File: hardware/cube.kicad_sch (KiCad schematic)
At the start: 16 parts, among them J1 PDB, M1 GM4108H, M2 Servo, SW1 Button, U1 ESP32-DevKitC, U2 BNO085, U3 Servo buck

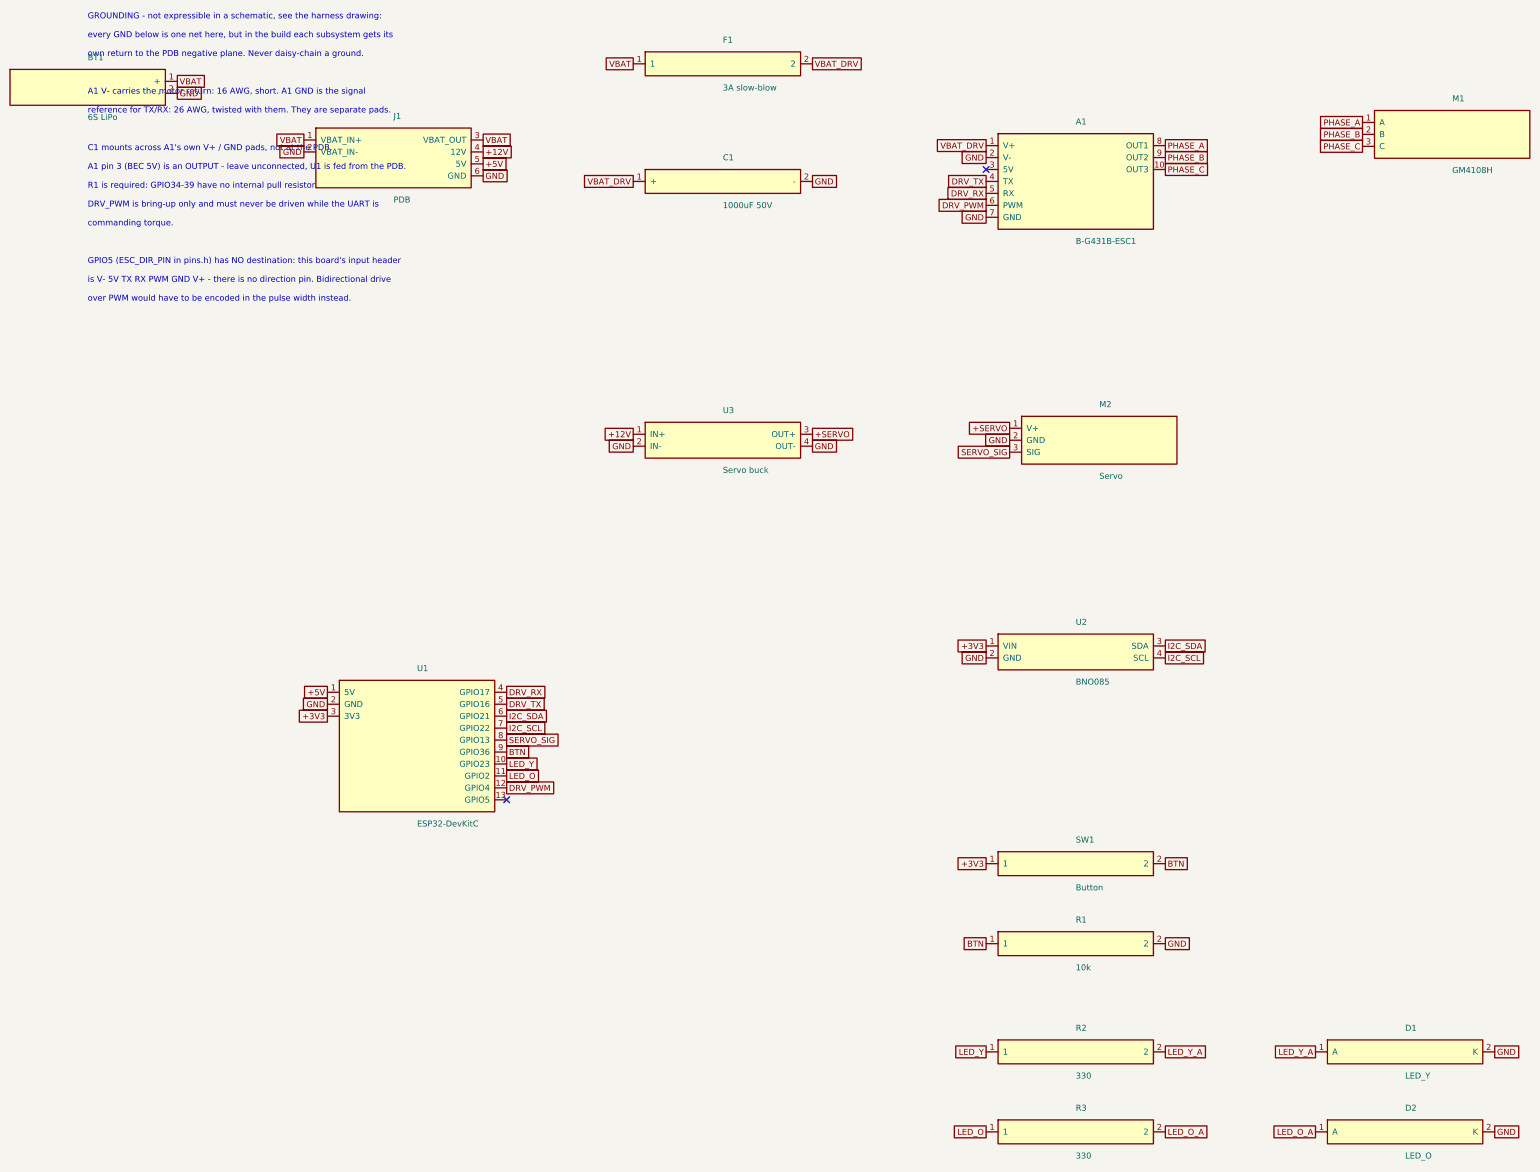
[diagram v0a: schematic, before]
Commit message: Redraw the schematic: real glyphs, drawn power chain, debug parts removed
The first sheet was a correct netlist and a poor drawing. Every part was a
rectangle and every connection was a matching pair of text labels, so the
topology could not be read - you could not see that C1 sits across the driver's
terminals, only infer it from two labels that happened to agree.

Changes:

- Passives carry their real symbols. BT1 is alternating cell plates, C1 is a
  polarised capacitor with its plates and + marker, F1 is the fuse glyph, M1 is
  a circle. The modules stay rectangles, which is correct: the PDB, driver,
  buck, IMU and ESP32 are finished boards you wire to, so a connector is the
  honest representation.

- The power chain is drawn with wires and junction dots, battery through PDB,
  fuse and bulk cap to the driver, so C1 is visibly in parallel across V+ and
  GND rather than implied.

- Rails use power symbols - a GND triangle, +5V / +3V3 / +12V bars - instead of
  text labels. Signals still travel by global label, which is ordinary practice
  and keeps the sheet legible.

- Removed the button, its pulldown, both LEDs and their series resistors. They
  are bring-up aids, not part of the machine. Removed the notes block; what it
  said about grounding belongs in the harness drawing, which is where the star
  topology and the wire gauges already live.

Both no-connects are kept, since each records a real finding: A1 pin 7 is the
BEC output and must not meet the PDB's 5 V rail, and U1 GPIO5 is ESC_DIR_PIN in
pins.h with no destination, because this driver's header has a PWM input and no
direction pin.

Checked: parentheses balanced outside strings, 159 unique UUIDs, every lib_id
defined, no duplicate symbol bodies, and all 46 part pins plus all 14 power
symbol pins terminate on a wire, a label or a no-connect - nothing dangles.
Not opened in KiCad; there is no install here.

Co-Authored-By: Claude Opus 5 <noreply@anthropic.com>
Claude-Session: https://claude.ai/code/s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
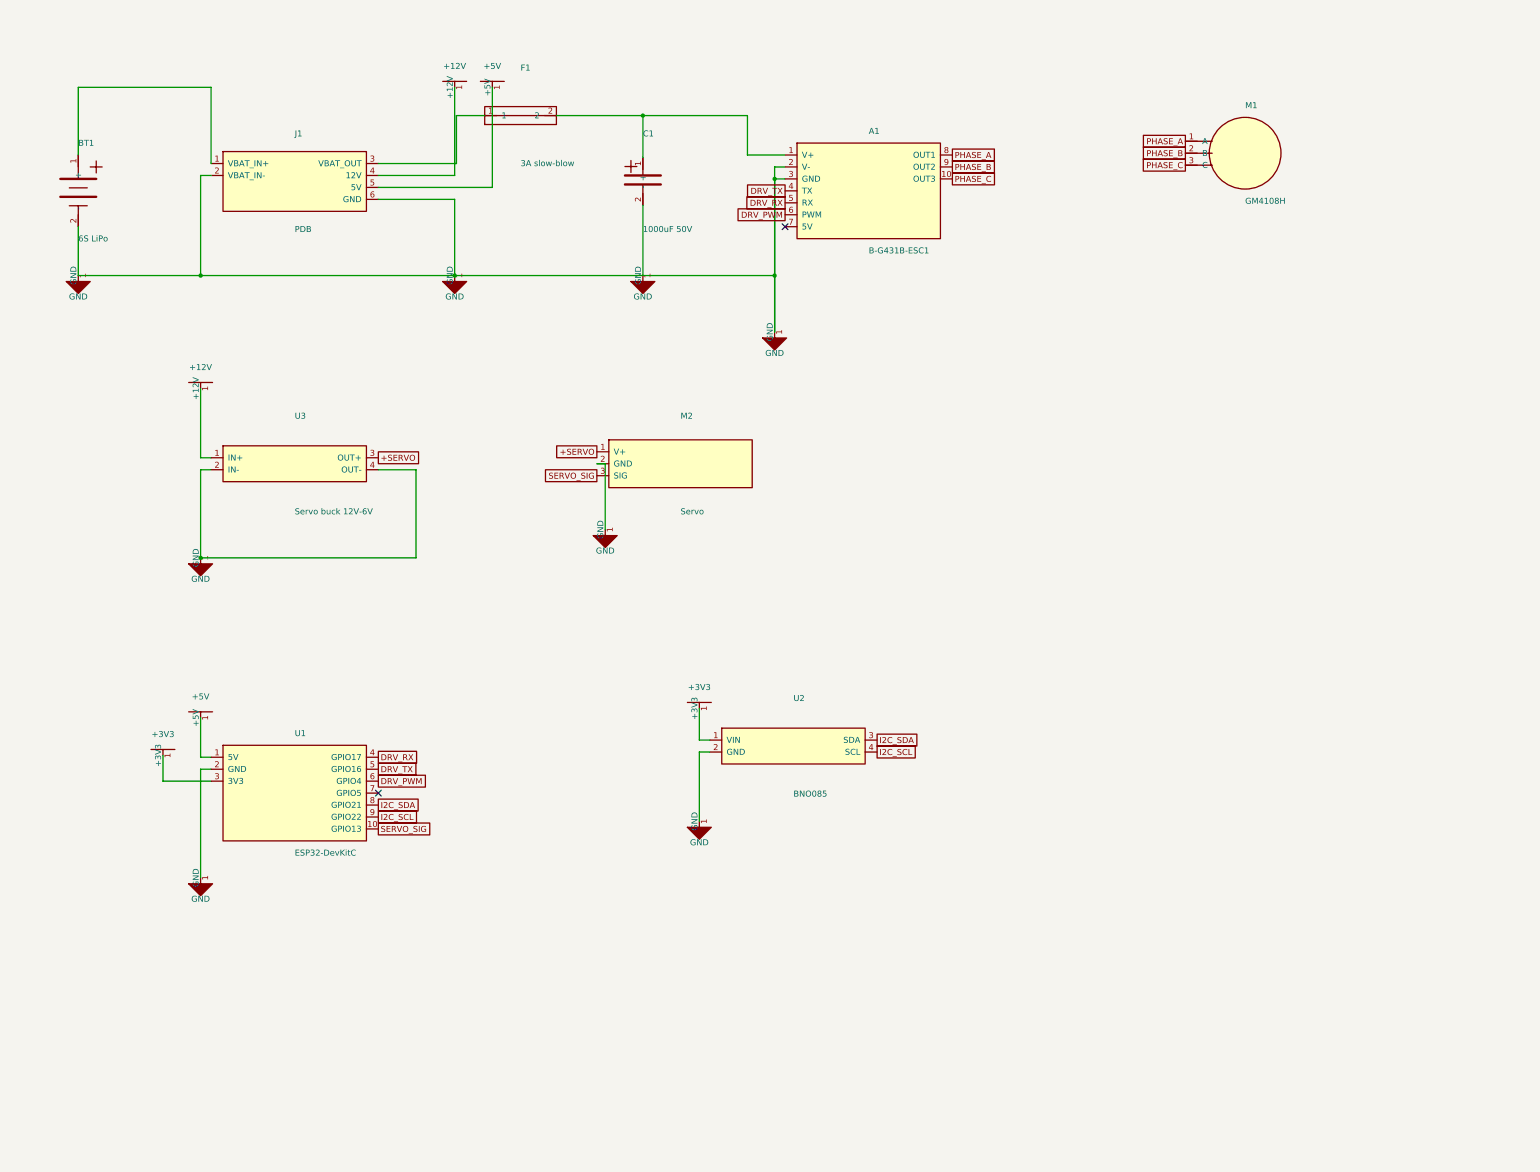
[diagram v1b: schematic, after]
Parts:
- removed D1: LED_Y, symbol cube:D_D1
- removed D2: LED_O, symbol cube:D_D2
- removed R1: 10k, symbol cube:R_R1
- removed R2: 330, symbol cube:R_R2
- removed R3: 330, symbol cube:R_R3
- removed SW1: Button, symbol cube:SW_SW1
- U3: value Servo buck -> Servo buck 12V-6V
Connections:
- net BTN is gone; now on net I2C_SCL: U1.9 (GPIO22)
- net LED_Y is gone; now on net SERVO_SIG: U1.10 (GPIO13)
- net DRV_PWM: now also U1.6 (GPIO4); no longer U1.12 (GPIO4)
- net GND: now also A1.3 (GND); no longer A1.7 (GND)
- net I2C_SCL: no longer U1.7 (GPIO22)
- net I2C_SDA: now also U1.8 (GPIO21); no longer U1.6 (GPIO21)
- net SERVO_SIG: no longer U1.8 (GPIO13)
- removed net LED_O: U1.11 (GPIO2)
- net VBAT: no longer names the net of BT1.1 (+), J1.1 (VBAT_IN+)
- net VBAT: no longer F1.1, J1.3 (VBAT_OUT)
- net VBAT_DRV: no longer names the net of A1.1 (V+), C1.1 (+), F1.2
- new net: F1.1, J1.3 (VBAT_OUT)
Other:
- note removed: "A1 V- carries the motor return: 16 AWG, short. A1 GND is the signal"
- note removed: "A1 pin 3 (BEC 5V) is an OUTPUT - leave unconnected, U1 is fed from the PDB."
- note removed: "C1 mounts across A1's own V+ / GND pads, not at the PDB."
- note removed: "DRV_PWM is bring-up only and must never be driven while the UART is"
- note removed: "GPIO5 (ESC_DIR_PIN in pins.h) has NO destination: this board's input header"
- note removed: "GROUNDING - not expressible in a schematic, see the harness drawing:"
- note removed: "R1 is required: GPIO34-39 have no internal pull resistor."
- note removed: "commanding torque."
- note removed: "every GND below is one net here, but in the build each subsystem gets its"
- note removed: "is V- 5V TX RX PWM GND V+ - there is no direction pin. Bidirectional drive"
- note removed: "over PWM would have to be encoded in the pulse width instead."
- note removed: "own return to the PDB negative plane. Never daisy-chain a ground."
- note removed: "reference for TX/RX: 26 AWG, twisted with them. They are separate pads."

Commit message: Drop the ground bus, tidy the rails, fix the power symbol text
Three fixes, all from reading the rendered sheet.

The drawn ground bus is gone. A schematic's GND is one node with zero impedance
between its pins - it has no topology - so drawing it as a line implied a
physical arrangement the sheet cannot express, which is misleading rather than
merely untidy. The real topology lives in the harness drawing. Ground pins now
carry a GND symbol directly, with a short dog-leg only where two symbols would
otherwise overlap. That removed 21 wires.

The power symbol's Value sat level with its own glyph, so "GND" printed over
the triangle and could not be moved from the instance, because the position
comes from the symbol definition. It now sits below the triangle's tip, and
above the bar for a rail.

Pin numbers and names are off for the passives: a battery needs no "pin 1".
Hidden via pin_numbers at symbol level and a "~" pin name, rather than the
per-field hide flag, which this KiCad was plainly ignoring.

Layout around the PDB was crossing itself. Rails now leave J1 on their own
dog-legs with the outer pin turning at the larger X, which is the condition for
two parallel runs not to cross, and U1's left pins are reordered 5V / 3V3 / GND
for the same reason. The battery, PDB, fuse and driver V+ now sit on one line,
so that run is straight with no bends at all.

Checked: parentheses balanced, 139 unique UUIDs, every lib_id defined, no
dangling pins, and no horizontal/vertical pair crossing without a junction
(shared corners excluded). One junction remains, where C1 branches off the V+
run - which is the connection worth seeing.

Co-Authored-By: Claude Opus 5 <noreply@anthropic.com>
Claude-Session: https://claude.ai/code/session_016JpVBg7jcYmKKG1BBj9Xst
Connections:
- net +3V3: now also U1.2 (3V3); no longer U1.3 (3V3)
- net GND: now also U1.3 (GND); no longer U1.2 (GND)
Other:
- moved on the sheet: A1, J1
